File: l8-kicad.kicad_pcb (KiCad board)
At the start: 4 copper layers, 56 x 90 mm, 91 parts, among them J1 USB_B_Mini, J2 LCD 3.2" 240x320 Conn_01x14_P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, J3 Screw_Terminal_01x06, J4 Conn_ST_STDC14, J5 Conn_02x05_Counter_Clockwise, J7 TC2030 - TAG Connect, Q2 S8550, Q3 S8550, SW1 SW_Push, SW2 SW_Push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

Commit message: x
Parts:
- moved R10 37.9 mm to (62.2, 43.5)
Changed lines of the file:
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@@
 	(footprint "Resistor_SMD:R_0603_1608Metric"
 		(layer "F.Cu")
-		(at 100 46.325 -90)
+		(at 62.25 43.475 -90)
 		(descr "Resistor SMD 0603 (1608 Metric), square (rectangular) end terminal, IPC_7351 nominal, (Body size source: IPC-SM-782 page 72, https://www.pcb-3d.com/wordpress/wp-content/uploads/ipc-sm-782a_amendment_1_and_2.pdf), generated with kicad-footprint-generator")
 		(tags "resistor")

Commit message: change power add buzzer
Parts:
- removed Q2, Q3: S8550, Package_TO_SOT_SMD:SOT-23
- added BZ1: Buzzer, dnt:Buzzer_9x9.5RM5.0, F.Cu at (64.5, 131.3)
- added Q1: SI2301CDS-T1-GE3, Package_TO_SOT_SMD:SOT-23, F.Cu at (61.5, 101.4)
- added Q4: SI2301CDS-T1-GE3, Package_TO_SOT_SMD:SOT-23, F.Cu at (68.4, 101.4)
- added Q5: SI2301CDS-T1-GE3, Package_TO_SOT_SMD:SOT-23, F.Cu at (48.5, 118.8)
- added R30: 100R, Resistor_SMD:R_0603_1608Metric, F.Cu at (61.1, 104.8)
- added R34: 1k, Resistor_SMD:R_0603_1608Metric, F.Cu at (68.0, 104.8)
- added R35: 100R, Resistor_SMD:R_0603_1608Metric, F.Cu at (66.0, 93.6)
- R13: value 1k -> R100
- R4: value 1k -> 100R
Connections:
- net /5V renamed +5V
- C11 pad 1: /SENSOR_VDD -> +3.3V
- C11 pad 2: GND -> Net-(Q1-D)
- C12 pad 1: /SENSOR_VDD -> +3.3V
- C12 pad 2: GND -> Net-(Q1-D)
- C30 pad 2: /VDD -> +3.3V
- C31 pad 2: /VDD -> +3.3V
- C32 pad 2: /VDD -> +3.3V
- C33 pad 2: /VDD -> +3.3V
- C34 pad 2: /VDD -> +3.3V
- C5 pad 2: /VDD -> +3.3V
- C6 pad 1: /VDD -> +3.3V
- C7 pad 1: /VDD -> +3.3V
- C9 pad 2: /VDD -> +3.3V
- D1 pad 2: /VDD -> +3.3V
- D8 pad 2: /VDD_SENSOR -> +3.3V
- D9 pad 2: /VDD_LCD -> +3.3V
- FB1 pad 1: /VDD -> +3.3V
- J2 pad 1: /VDD_LCD -> +3.3V
- J2 pad 2: GND -> Net-(J2-GND)
- J4 pad 11: GND -> Net-(J4-GNDDetect)
- J4 pad 3: /VDD -> +3.3V
- J5 pad 2: /VDD -> +3.3V
- J7 pad 1: /VDD -> +3.3V
- R10 pad 1: GND -> Net-(Q1-D)
- R11 pad 1: GND -> Net-(Q1-D)
- R12 pad 1: GND -> Net-(Q1-D)
- R13 pad 1: GND -> /SENSOR_ON
- R13 pad 2: Net-(D8-K) -> Net-(Q1-G)
- R15 pad 2: /SENSOR_VDD -> +3.3V
- R43 pad 1: /VDD -> +3.3V
- R7 pad 2: /SENSOR_VDD -> +3.3V
- R8 pad 2: /SENSOR_VDD -> +3.3V
- R9 pad 1: GND -> Net-(Q1-D)
- SW1 pad 1: /VDD -> +3.3V
- U2 pad 1: /VDD -> +3.3V
- U22 pad 1: /VDD -> +3.3V
- U22 pad 2: /VDD -> +3.3V
- U3 pad 100: /VDD -> +3.3V
- U3 pad 11: /VDD -> +3.3V
- U3 pad 19: /VDD -> +3.3V
- U3 pad 28: /VDD -> +3.3V
- U3 pad 44: unconnected-(U3-PE13-Pad44) -> /MCU/BEEPER
- U3 pad 50: /VDD -> +3.3V
- U3 pad 6: /VDD -> +3.3V
- U3 pad 75: /VDD -> +3.3V
- U4 pad 1: /SENSOR_VDD -> +3.3V
- U4 pad 13: GND -> Net-(Q1-D)
- U4 pad 2: /SENSOR_VDD -> +3.3V
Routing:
- added copper zone on In2.Cu, net +3.3V
- removed copper zone on In2.Cu, net /VDD

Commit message: remove hellen
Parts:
- added R2: 10K, Resistor_SMD:R_0603_1608Metric, F.Cu at (210.0, 44.3)
- added R3: 100R, Resistor_SMD:R_0603_1608Metric, F.Cu at (210.0, 48.8)
- added R32: 100R, Resistor_SMD:R_0603_1608Metric, F.Cu at (204.0, 44.3)
- added R33: 10K, Resistor_SMD:R_0603_1608Metric, F.Cu at (204.0, 46.8)
- R14: value 1k -> 10K
- U1: footprint footprints:B0505S-1WR2_MNS -> dnt:B0505S-1WR2_MNS
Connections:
- R14 pad 2: Net-(D9-K) -> Net-(Q4-G)

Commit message: x
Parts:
- removed J5: Conn_02x05_Counter_Clockwise, Connector_PinHeader_2.54mm:PinHeader_2x05_P2.54mm_Vertical_SMD
- moved PS1 58.8 mm to (156.3, 29.2)
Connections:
- J7 pad 1: +3.3V -> /MCU/VDD
- R33 pad 1: unconnected-(R33-Pad1) -> GND
- R33 pad 2: unconnected-(R33-Pad2) -> Net-(Q5-G)
- R43 pad 1: +3.3V -> /MCU/VDD
- SW1 pad 1: +3.3V -> /MCU/VDD
- U3 pad 47: unconnected-(U3-PB10-Pad47) -> /MCU/PB10
- U3 pad 48: unconnected-(U3-PB11-Pad48) -> /MCU/PB11
- U3 pad 51: unconnected-(U3-PB12-Pad51) -> /MCU/PB12
- U3 pad 95: unconnected-(U3-PB8-Pad95) -> /MCU/PB8
- U3 pad 96: unconnected-(U3-PB9-Pad96) -> /MCU/PB9
- U5 pad 10: GND -> Net-(Q1-D)
- U5 pad 11: GND -> Net-(Q1-D)
- U5 pad 12: GND -> Net-(Q1-D)
- U5 pad 13: GND -> Net-(Q1-D)
- U5 pad 14: GND -> Net-(Q1-D)
- U5 pad 15: GND -> Net-(Q1-D)
- U5 pad 16: GND -> Net-(Q1-D)
- U5 pad 7: /SENSOR_VDD -> +3.3V
- U5 pad 8: /SENSOR_VDD -> +3.3V
- U5 pad 9: GND -> Net-(Q1-D)

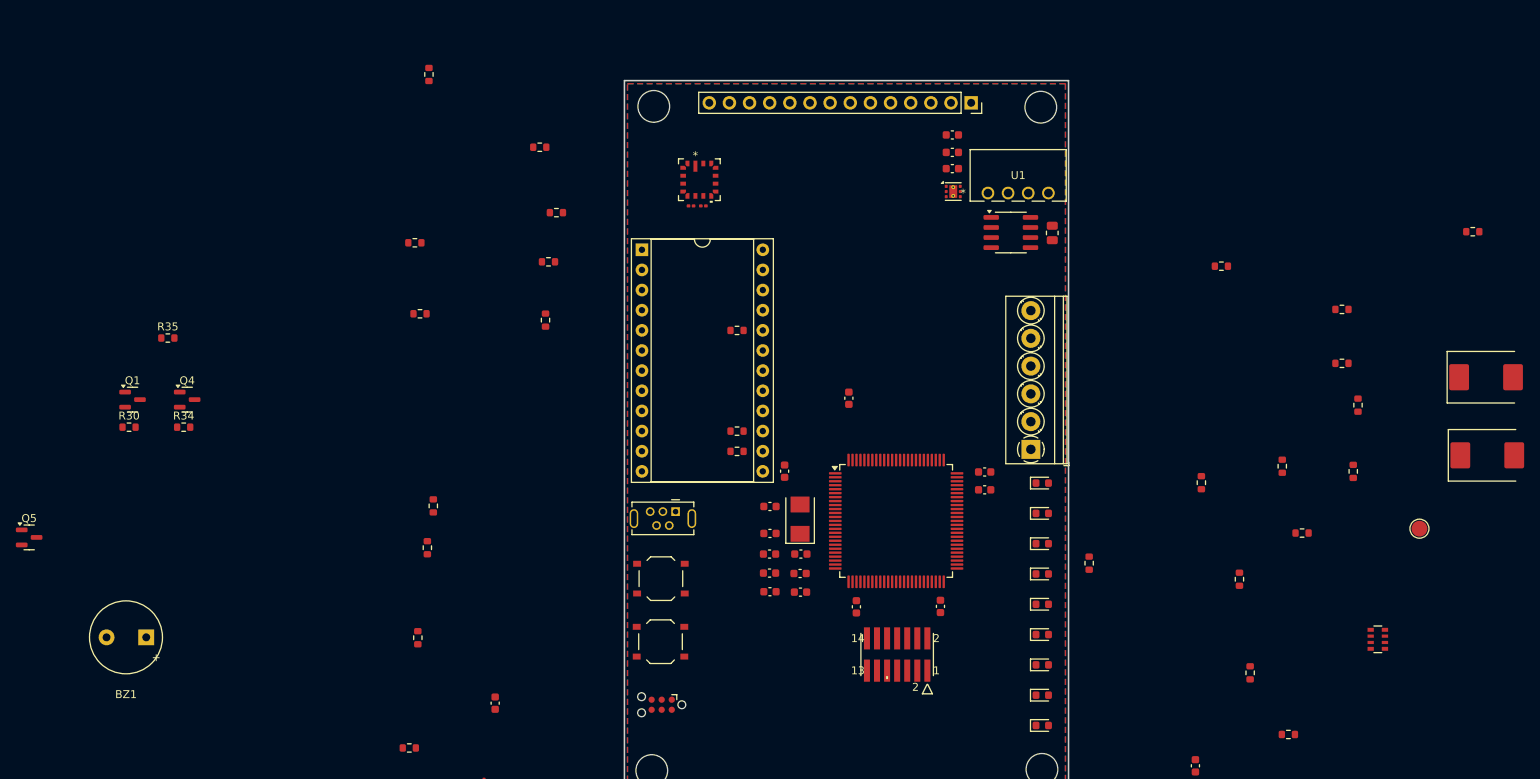
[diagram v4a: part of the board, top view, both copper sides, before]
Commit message: finalise debug header and test points
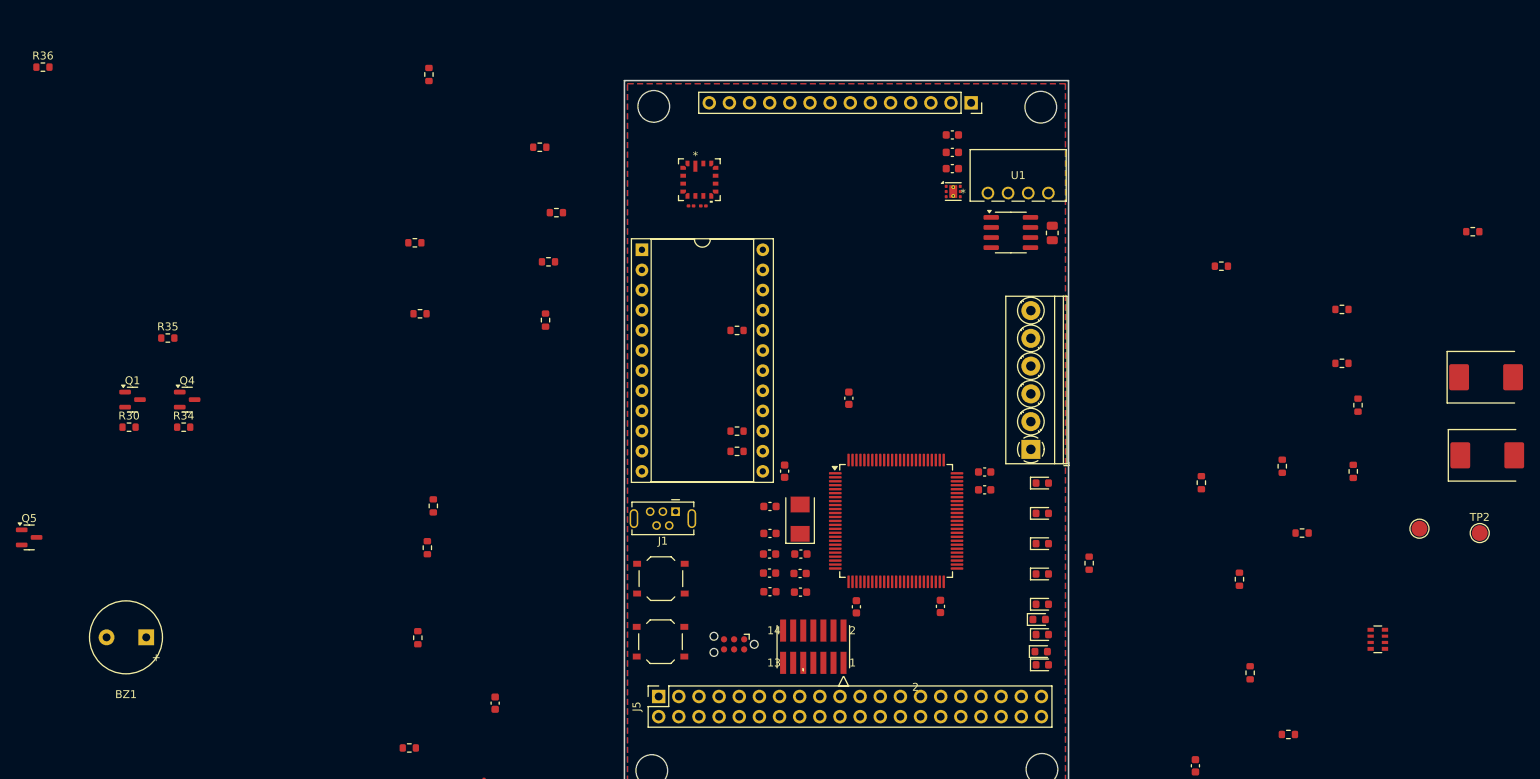
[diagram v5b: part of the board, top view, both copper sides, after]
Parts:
- added J5: Conn_02x20_Odd_Even, Connector_PinSocket_2.54mm:PinSocket_2x20_P2.54mm_Vertical, F.Cu at (127.9, 138.8)
- added R36: 10K, Resistor_SMD:R_0603_1608Metric, F.Cu at (50.2, 59.5)
- added TP2: 5V, TestPoint:TestPoint_Pad_D2.0mm, F.Cu at (231.4, 118.2)
- J1: footprint hellen-one-common:USB-MINI-B-VERTICAL -> dnt:USB-MINI-B-VERTICAL
- moved D9 13.4 mm to (175.8, 129.1)
- moved J7 11.9 mm to (137.4, 132.2)
- moved J4 10.6 mm to (147.4, 132.5)
- moved D7 5.49 mm to (176.1, 133.2)
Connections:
- D16 pad 5: /MCU/5V -> +5V
- D17 pad 1: /MCU/5V -> +5V
- J7 pad 1: /MCU/VDD -> +3.3V
- R43 pad 1: /MCU/VDD -> +3.3V
- SW1 pad 1: /MCU/VDD -> +3.3V
- U3 pad 15: unconnected-(U3-PC0-Pad15) -> /MCU/PC0
- U3 pad 23: unconnected-(U3-PA0-Pad23) -> /MCU/PA0
- U3 pad 24: unconnected-(U3-PA1-Pad24) -> /MCU/PA1
- U3 pad 29: unconnected-(U3-PA4-Pad29) -> /MCU/PA4
- U3 pad 37: GND -> /MCU/BOOT1
- U3 pad 38: unconnected-(U3-PE7-Pad38) -> /MCU/PE7
- U3 pad 39: unconnected-(U3-PE8-Pad39) -> /MCU/PE8
- U3 pad 40: unconnected-(U3-PE9-Pad40) -> /MCU/PE9
- U3 pad 41: unconnected-(U3-PE10-Pad41) -> /MCU/PE10
- U3 pad 42: unconnected-(U3-PE11-Pad42) -> /MCU/PE11
- U3 pad 43: unconnected-(U3-PE12-Pad43) -> /MCU/PE12
- U3 pad 55: unconnected-(U3-PD8-Pad55) -> /MCU/PD8
- U3 pad 56: unconnected-(U3-PD9-Pad56) -> /MCU/PD9
- U3 pad 57: unconnected-(U3-PD10-Pad57) -> /MCU/PD10
- U3 pad 58: unconnected-(U3-PD11-Pad58) -> /MCU/PD11
- U3 pad 63: unconnected-(U3-PC6-Pad63) -> /MCU/PC6
- U3 pad 64: unconnected-(U3-PC7-Pad64) -> /MCU/PC7
- U3 pad 65: unconnected-(U3-PC8-Pad65) -> /MCU/PC8
- U3 pad 66: unconnected-(U3-PC9-Pad66) -> /MCU/PC9
- U3 pad 67: unconnected-(U3-PA8-Pad67) -> /MCU/PA8
- U3 pad 7: unconnected-(U3-PC13-Pad7) -> /MCU/PC13
- U3 pad 8: unconnected-(U3-PC14-Pad8) -> /MCU/PC14
- U3 pad 87: unconnected-(U3-PD6-Pad87) -> /MCU/PD6
- U3 pad 88: unconnected-(U3-PD7-Pad88) -> /MCU/PD7
- U3 pad 9: unconnected-(U3-PC15-Pad9) -> /MCU/PC15
- U3 pad 90: unconnected-(U3-PB4-Pad90) -> /MCU/PB4
- U3 pad 91: unconnected-(U3-PB5-Pad91) -> /MCU/PB5
- U3 pad 97: unconnected-(U3-PE0-Pad97) -> /MCU/PE0
- U3 pad 98: unconnected-(U3-PE1-Pad98) -> /MCU/PE1

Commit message: xq
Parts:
- added TP3: IIS3DHHCTR_SDI, TestPoint:TestPoint_Pad_D2.0mm, F.Cu at (83.8, 183.8)
- added TP4: IIS3DHHCTR_SDI, TestPoint:TestPoint_Pad_D2.0mm, F.Cu at (73.5, 173.4)
- added TP5: IIS3DHHCTR_SCK, TestPoint:TestPoint_Pad_D2.0mm, F.Cu at (73.5, 177.5)
- added TP6: 5V ISO, TestPoint:TestPoint_Pad_D2.0mm, F.Cu at (74.0, 184.2)
- added TP7: GND ISO, TestPoint:TestPoint_Pad_D2.0mm, F.Cu at (79.2, 184.2)
- TP2: value 5V -> +3.3V
- moved R12 124.8 mm to (26.3, 164.0)
- moved R23 108.2 mm to (37.8, 51.2)
- moved R11 107.8 mm to (31.8, 85.8)
- moved PS1 99.6 mm to (143.5, 127.9)
- moved FB1 90.8 mm to (31.8, 97.1)
- moved R9 63.4 mm to (69.2, 67.9)
- moved R43 59.7 mm to (231.2, 155.9)
- moved J7 49.7 mm to (105.0, 170.0)
- moved J4 49.4 mm to (115.8, 170.5)
- moved C5 47.8 mm to (140.9, 109.4)
- moved C6 47.8 mm to (140.9, 113.7)
- moved C7 47.8 mm to (140.9, 111.6)
- moved R1 47.8 mm to (153.6, 121.8)
- moved U2 47.8 mm to (148.3, 121.7)
- moved U1 47.8 mm to (145.4, 116.7)
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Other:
- board size 56 x 90 mm -> 55.5 x 89.5 mm
- board text added: "+3.3V"
- board text added: "+5V"
- board text added: "LCDP"
- board text added: "PD12"
- board text added: "PD13"
- board text added: "PD14"
- board text added: "PD15"
- board text added: "SENP"
- board text added: "USBP"
- board text added: "l8-console"
- board text removed: "2"

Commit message: pre quilter
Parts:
- added R37: 10K, Resistor_SMD:R_0603_1608Metric, F.Cu at (168.8, 26.0)
- added R38: 10K, Resistor_SMD:R_0603_1608Metric, F.Cu at (168.8, 28.5)
- added R39: 10K, Resistor_SMD:R_0603_1608Metric, F.Cu at (168.8, 31.0)
- moved TP1 162.8 mm to (68.0, 165.0)
- moved TP2 162.8 mm to (75.6, 165.6)
- moved J7 0.70 mm to (104.8, 170.6)
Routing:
- net /VBATT: track 0.00 -> 56.5 mm
- removed copper zone on In2.Cu, net +3.3V
- removed copper zone on B.Cu, net GND
- removed copper zone on F.Cu, net GND
- removed copper zone on In1.Cu, net GND
